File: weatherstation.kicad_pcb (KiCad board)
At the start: 2 copper layers, 126 parts, among them J1 Conn_02x05_Odd_Even, J2 Conn_02x10_Odd_Even, Q1 NX3020NAK, Q2 NX3020NAK, Q3 FDS86267P, Q4 TN2404K-T1-E3, SW1 SW_Push, U1 IS25LP064A-JBLE, U10 74AHC1G04, U11 ISL3330, U12 CPC1017N, U13 CPC1017N, U14 LM22675, U15 TPS793333-EP, U16 TPS54202, U2 MAX3221ECPWR, U3 STM32F091C(B-C)Tx_u, U4 LIS2DE12, U5 ADS1120-PW, U6 2SMPB-02E, U7 SHT3x-DIS, U8 ADA4528-1, U9 MCP2542-E/SN, X1 DSC1001CI1-004.0960T, Y1 8MHz, Y2 32.768kHz

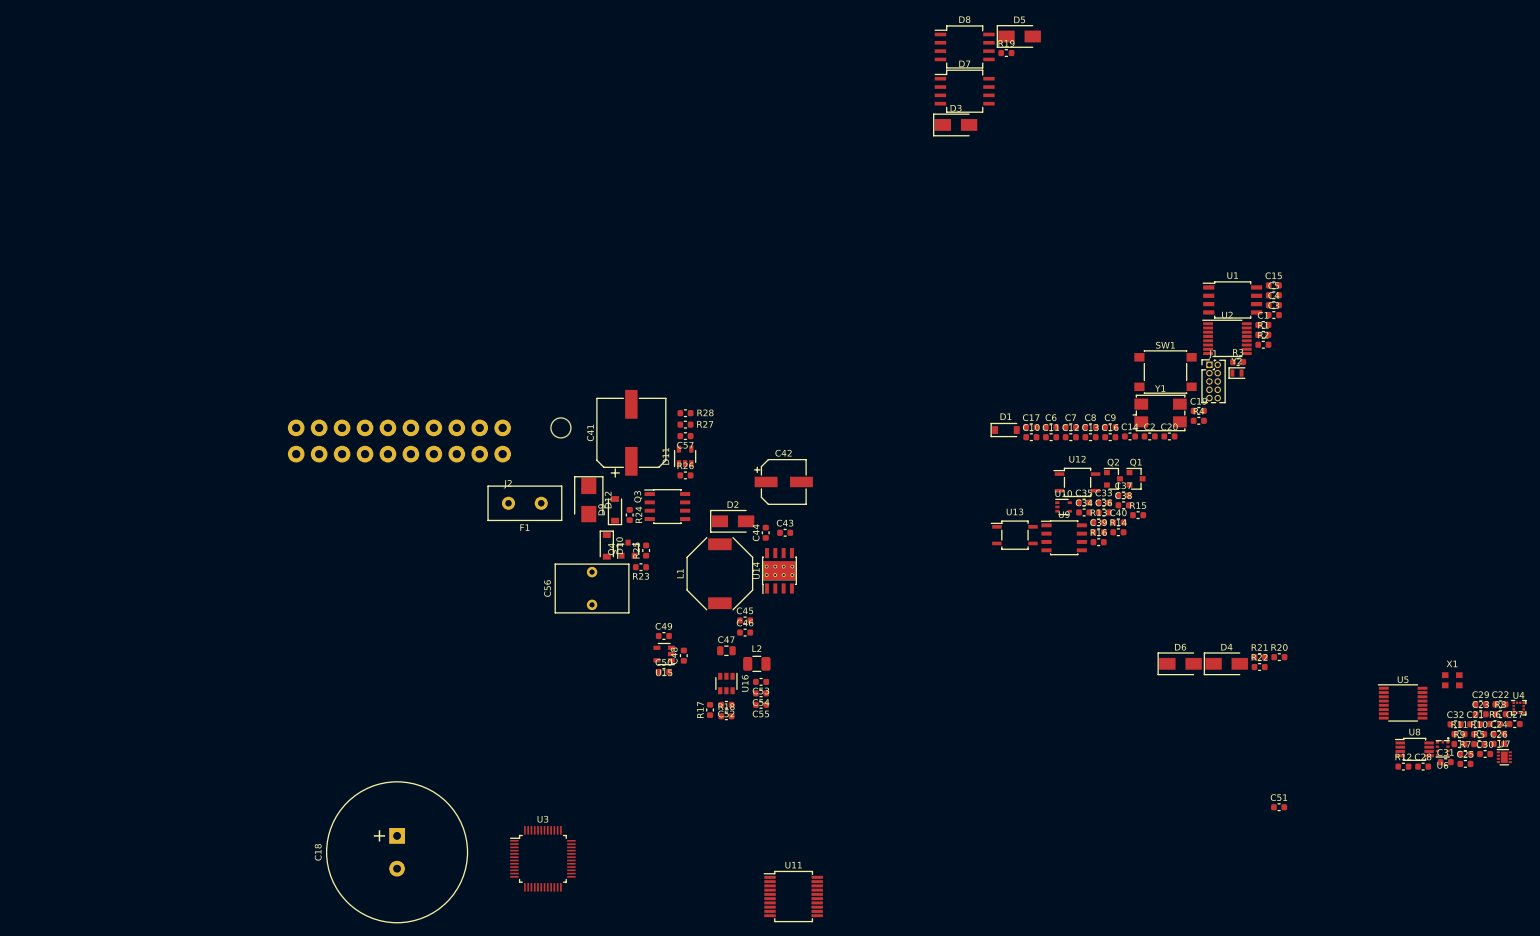
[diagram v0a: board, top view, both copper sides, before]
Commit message: Initial schematic work for rock64 version
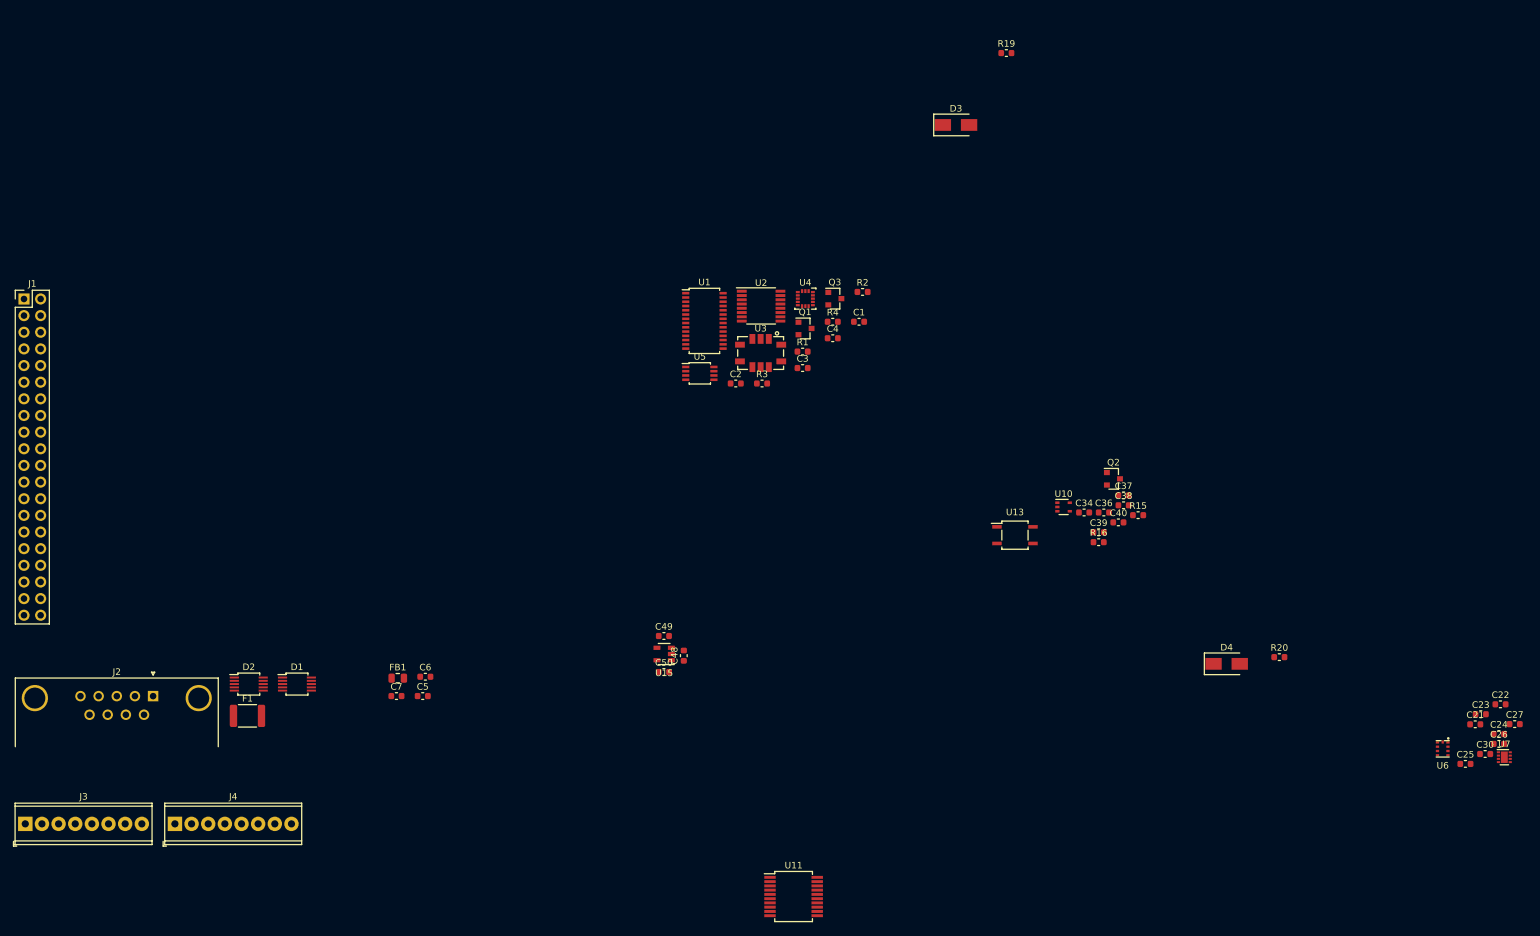
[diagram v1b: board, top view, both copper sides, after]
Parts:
- removed C10, C15, C19, C28, C32, C33, C35, C51, C57, C8, C9: 100nF, Capacitor_SMD:C_0603_1608Metric
- removed C11, C14: 26pF, Capacitor_SMD:C_0603_1608Metric
- removed C12, C29, C43: 1uF, Capacitor_SMD:C_0603_1608Metric
- removed C13, C44: 10nF, Capacitor_SMD:C_0603_1608Metric
- removed C16: 4.7uF, Capacitor_SMD:C_0603_1608Metric
- removed C17, C20: 2pF, Capacitor_SMD:C_0603_1608Metric
- removed C18: 1F, supercap:CP_Radial_D21.5mm_P5.00mm
- removed C31: 10pF, Capacitor_SMD:C_0603_1608Metric
- removed C41: 180uF, Capacitor_SMD:CP_Elec_10x12.6
- removed C42: 47uF, Capacitor_SMD:CP_Elec_6.3x7.7
- removed C45, C46, C53, C54, C55: 22uF, Capacitor_SMD:C_0603_1608Metric
- removed C47: 33uF, Capacitor_SMD:C_0805_2012Metric
- removed C52: 56pF, Capacitor_SMD:C_0603_1608Metric
- removed C56: 10uF, Capacitor_THT:C_Rect_L7.2mm_W11.0mm_P5.00mm_FKS2_FKP2_MKS2_MKP2
- removed D10, D9: PDZ5.6BGWJ, Diode_SMD:D_SOD-123
- removed D11: TL431DBV, Package_TO_SOT_SMD:SOT-23-5
- removed D12: STPS3170UF, Diode_SMD:D_SMB
- removed D5, D6: WE_824501361, Diode_SMD:D_SMA
- removed D7, D8: CM1213A-06SO, Package_SO:SO-8_5.3x6.2mm_P1.27mm
- removed L1: 33uH, inductor_sru1048:L_Bourns_SRU1048
- removed L2: 4.7uH, inductor_1008_2520:L_1008_2520Metric
- removed Q4: TN2404K-T1-E3, Package_TO_SOT_SMD:SOT-23
- removed R10, R11, R18, R8, R9: 100k, Resistor_SMD:R_0603_1608Metric
- removed R12: 1k, Resistor_SMD:R_0603_1608Metric
- removed R13: 2.1k, Resistor_SMD:R_0603_1608Metric
- removed R14: 84.5, Resistor_SMD:R_0603_1608Metric
- removed R17: 22.1k, Resistor_SMD:R_0603_1608Metric
- removed R21, R22: 10, Resistor_SMD:R_0603_1608Metric
- removed R23: 15k, Resistor_SMD:R_0603_1608Metric
- removed R24, R25, R26, R28, R7: 10k, Resistor_SMD:R_0603_1608Metric
- removed R27: 68k, Resistor_SMD:R_0603_1608Metric
- removed R5: 1, Resistor_SMD:R_0603_1608Metric
- removed R6: 23k, Resistor_SMD:R_0603_1608Metric
- removed SW1: SW_Push, Button_Switch_SMD:SW_SPST_PTS645
- removed U12: CPC1017N, Package_SO:SOP-4_3.8x4.1mm_P2.54mm
- removed U14: LM22675, Package_SO:Texas_HSOP-8-1EP_3.9x4.9mm_P1.27mm_ThermalVias
- removed U16: TPS54202, Package_TO_SOT_SMD:SOT-23-6
- removed U8: ADA4528-1, Package_SO:MSOP-8_3x3mm_P0.65mm
- removed U9: MCP2542-E/SN, Package_SO:SOIC-8_3.9x4.9mm_P1.27mm
- removed X1: DSC1001CI1-004.0960T, Oscillator:Oscillator_SMD_EuroQuartz_XO32-4Pin_3.2x2.5mm
- removed Y1: 8MHz, Crystal:Crystal_SMD_7050-4Pin_7.0x5.0mm
- removed Y2: 32.768kHz, Crystal:Crystal_SMD_2012-2Pin_2.0x1.2mm
- added FB1: 180R/100M, Inductor_SMD:L_0805_2012Metric, F.Cu at (105.6, 130.7)
- added J3: Screw_Terminal_01x08, TerminalBlock_Phoenix:TerminalBlock_Phoenix_MPT-0,5-8-2.54_1x08_P2.54mm_Horizontal, F.Cu at (48.8, 152.9)
- added J4: Screw_Terminal_01x08, TerminalBlock_Phoenix:TerminalBlock_Phoenix_MPT-0,5-8-2.54_1x08_P2.54mm_Horizontal, F.Cu at (71.6, 152.9)
- C2: value 100nF -> 4.7uF
- C21: value 10uF -> 4.7uF
- C5, C6: value 100nF -> 22uF
- C7: value 4.7uF -> 100nF
- D1: value BAT54GW -> CM1213A-08SO; footprint Diode_SMD:D_SOD-123 -> Package_SO:MSOP-10_3x3mm_P0.5mm
- D2: value MBRA160T3G -> CM1213A-08SO; footprint Diode_SMD:D_SMA -> Package_SO:MSOP-10_3x3mm_P0.5mm
- F1: value 0ZRC0160FF1A -> PFMF.030.2; footprint Capacitor_THT:C_Disc_D11.0mm_W5.0mm_P5.00mm -> Resistor_SMD:R_1812_4532Metric
- J1: value Conn_02x05_Odd_Even -> Conn_02x20_Odd_Even; footprint Connector_PinHeader_1.27mm:PinHeader_2x05_P1.27mm_Vertical -> Connector_PinHeader_2.54mm:PinHeader_2x20_P2.54mm_Vertical
- J2: value Conn_02x10_Odd_Even -> DB9_Female_MountingHoles; footprint cinch_enclosure:Cinch_ 5810120011_large -> Connector_Dsub:DSUB-9_Female_Horizontal_P2.77x2.84mm_EdgePinOffset4.94mm_Housed_MountingHolesOffset7.48mm
- Q3: value FDS86267P -> PMV160UP; footprint Package_SO:SOIC-8_3.9x4.9mm_P1.27mm -> Package_TO_SOT_SMD:SOT-23
- R1: value 100k -> 237k 0.1%
- R16: value 84.5 -> 113
- R2: value 1k -> 82
- R3: value 221 -> 51
- R4: value 10k -> 82
- U1: value IS25LP064A-JBLE -> ADS1148-PW; footprint Package_SO:SOIJ-8_5.3x5.3mm_P1.27mm -> Package_SO:TSSOP-28_4.4x9.7mm_P0.65mm
- U15: value TPS793333-EP -> TPS793285-EP
- U2: value MAX3221ECPWR -> ADS112C04-PW
- U3: value STM32F091C(B-C)Tx_u -> MICS-4514; footprint Package_QFP:LQFP-48_7x7mm_P0.5mm -> MICS-4514:MICS-4514
- U4: value LIS2DE12 -> MMA8451Q; footprint Package_LGA:LGA-12_2x2mm_P0.5mm -> Package_LGA:LGA-16_3x3mm_P0.5mm_LayoutBorder3x5y
- U5: value ADS1120-PW -> LM75C; footprint Package_SO:TSSOP-16_4.4x5mm_P0.65mm -> Package_SO:TSSOP-8_3x3mm_P0.65mm
- moved J1 181.1 mm to (48.6, 72.8)
- moved C5 143.5 mm to (109.4, 133.4)
- moved U4 125.5 mm to (167.8, 72.8)
- moved U5 118.5 mm to (151.7, 84.2)
- moved D1 114.9 mm to (90.2, 131.6)
- moved C7 110.8 mm to (105.4, 133.4)
- moved C6 102.8 mm to (109.8, 130.5)
- moved U3 84.0 mm to (161.0, 81.1)
- moved U1 80.7 mm to (152.4, 76.2)
- moved D2 77.9 mm to (82.9, 131.6)
- moved J2 74.5 mm to (68.3, 133.4)
- moved R3 72.7 mm to (161.2, 85.7)
- moved C3 72.4 mm to (167.4, 83.4)
- moved U2 71.3 mm to (161.0, 73.9)
- moved R1 70.3 mm to (167.4, 80.9)
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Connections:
- C1 pad 1: Net-(C1-Pad1) -> +3V3
- C1 pad 2: Net-(C1-Pad2) -> GND
- C2 pad 2: Net-(C2-Pad2) -> GND
- C21 pad 1: +3.3VA -> +2V8
- C22 pad 1: +3.3VA -> +3V3
- C23 pad 1: +3.3VA -> Net-(C23-Pad1)
- C25 pad 1: +3.3VA -> +2V8
- C26 pad 1: +3.3VA -> +2V8
- C27 pad 1: +3.3VA -> +3V3
- C3 pad 1: +3V3 -> +2V8
- C4 pad 1: Net-(C4-Pad1) -> +3.3VA
- C48 pad 1: +5V -> +2V8
- C5 pad 1: Net-(C5-Pad1) -> +3.3VA
- C6 pad 1: +3V3 -> +3.3VA
- C7 pad 1: +3V3 -> +3.3VA
- D1 pad 1: Net-(D1-Pad1) -> (no net)
- D1 pad 2: +3V3 -> (no net)
- D2 pad 1: Net-(C44-Pad1) -> IEXC1
- D2 pad 2: GND -> IEXC2
- F1 pad 2: +VDC -> +5V
- J1 pad 10: /nRST -> (no net)
- J1 pad 2: /SWDIO -> +5V
- J1 pad 3: GND -> I2C0_SDA
- J1 pad 4: /SWCLK -> +5V
- J1 pad 5: GND -> I2C0_SCL
- J1 pad 6: Net-(J1-Pad6) -> GND
- J1 pad 7: Net-(J1-Pad7) -> (no net)
- J1 pad 8: Net-(J1-Pad8) -> (no net)
- J2 pad 1: +VDC -> (no net)
- J2 pad 2: GND -> /connectors/RS485_D-_ESD
- J2 pad 3: /connectors/CAN_H_ESD -> /connectors/RS485_D+_ESD
- J2 pad 4: /connectors/CAN_L_ESD -> (no net)
- J2 pad 5: /connectors/RS485_D-_ESD -> GND
- J2 pad 6: /connectors/RS485_D+_ESD -> (no net)
- J2 pad 7: DBG_TX -> (no net)
- J2 pad 8: DBG_RX -> (no net)
- J2 pad 9: ADC_IN6 -> (no net)
- Q1 pad 1: CAN_TERM -> SNSR_HEAT
- Q3 pad 1: Net-(C41-Pad1) -> ~SNSR_HEAT2
- Q3 pad 2: Net-(C41-Pad1) -> Net-(Q3-Pad2)
- Q3 pad 3: Net-(C41-Pad1) -> Net-(Q3-Pad3)
- R1 pad 1: CAN_STBY -> /sensors/afe/RsRED_Isrc
- R2 pad 1: Net-(D1-Pad1) -> +5V
- R2 pad 2: Net-(C18-Pad1) -> Net-(R2-Pad2)
- R3 pad 1: /RCC_OSC_OUT -> Net-(Q3-Pad2)
- R3 pad 2: Net-(C14-Pad1) -> Net-(Q3-Pad3)
- R4 pad 1: +3V3 -> +5V
- R4 pad 2: /nRST -> Net-(Q3-Pad2)
- U1 pad 1: SPI1_NSS -> +3V3
- U1 pad 2: SPI1_MISO -> GND
- U1 pad 3: +3V3 -> (no net)
- U1 pad 4: GND -> +3V3
- U1 pad 5: SPI1_MOSI -> REFP0
- U1 pad 6: SPI1_SCK -> REFN1
- U1 pad 7: +3V3 -> REFP1
- U1 pad 8: +3V3 -> REFN0
- U11 pad 15: USART2_TX -> (no net)
- U15 pad 1: +5V -> +2V8
- U15 pad 3: +5V -> +2V8
- U2 pad 10: Net-(U2-Pad10) -> /sensors/afe/RsOX_Isrc
- U2 pad 11: USART1_TX -> /sensors/afe/RsOX_Isrc
- U2 pad 12: GND -> +2V8
- U2 pad 13: DBG_TX -> +3V3
- U2 pad 14: GND -> ~DRDY_SNSR
- U2 pad 15: +3V3 -> I2C0_SCL
- U2 pad 16: +3V3 -> I2C0_SDA
- U2 pad 2: Net-(C1-Pad1) -> GND
- U2 pad 3: Net-(C4-Pad1) -> +3V3
- U2 pad 4: Net-(C1-Pad2) -> GND
- U2 pad 5: Net-(C2-Pad1) -> GND
- U2 pad 6: Net-(C2-Pad2) -> /sensors/afe/RsRED_Isrc
- U2 pad 7: Net-(C5-Pad1) -> /sensors/afe/RsRED_Isrc
- U2 pad 8: DBG_RX -> (no net)
- U2 pad 9: USART1_RX -> (no net)
- U4 pad 1: I2C1_SCL -> +3V3
- U4 pad 10: +3.3VA -> GND
- U4 pad 11: Net-(U4-Pad11) -> INT1_ACCEL
- U4 pad 12: INT1_ACCEL -> GND
- U4 pad 2: +3.3VA -> Net-(C23-Pad1)
- U4 pad 3: GND -> (no net)
- U4 pad 4: I2C1_SDA -> I2C0_SCL
- U4 pad 6: GND -> I2C0_SDA
- U4 pad 8: GND -> (no net)
- U4 pad 9: +3.3VA -> (no net)
- U5 pad 1: SPI2_SCK -> I2C0_SDA
- U5 pad 2: SPI2_NSS -> I2C0_SCL
- U5 pad 3: Net-(U5-Pad3) -> (no net)
- U5 pad 6: AFE_AIN3 -> GND
- U5 pad 7: AFE_AIN2 -> GND
- U5 pad 8: Net-(U5-Pad8) -> +3.3VA
- U6 pad 3: I2C1_SDA -> I2C0_SDA
- U6 pad 4: I2C1_SCL -> I2C0_SCL
- U6 pad 6: +3.3VA -> +3V3
- U6 pad 9: Net-(U6-Pad9) -> (no net)
- U7 pad 1: I2C1_SDA -> I2C0_SDA
- U7 pad 4: I2C1_SCL -> I2C0_SCL

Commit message: Revision A
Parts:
- removed C34: 100nF, Capacitor_SMD:C_0603_1608Metric
- removed U10: 74AHC1G04, Package_TO_SOT_SMD:SOT-353_SC-70-5
- added H1: MountingHole_Pad, MountingHole:MountingHole_2.7mm_M2.5_ISO14580_Pad, F.Cu at (33.5, 23.5)
- added H2: MountingHole_Pad, MountingHole:MountingHole_2.7mm_M2.5_ISO14580_Pad, F.Cu at (91.5, 23.5)
- added H3: MountingHole_Pad, MountingHole:MountingHole_2.7mm_M2.5_ISO14580_Pad, F.Cu at (91.5, 72.5)
- added H4: MountingHole_Pad, MountingHole:MountingHole_2.7mm_M2.5_ISO14580_Pad, F.Cu at (33.5, 72.5)
- added J5: Conn_02x11_Odd_Even, Connector_PinHeader_2.54mm:PinHeader_2x11_P2.54mm_Vertical, F.Cu at (43.6, 30.4)
- moved C24 228.9 mm to (60.5, 55.8), turned to 270 degrees
- moved R20 215.4 mm to (42.2, 42.2)
- moved C25 215.2 mm to (70.4, 59.7)
- moved C22 211.9 mm to (75.8, 59.2), turned to 270 degrees
- moved C21 210.9 mm to (75.8, 55.4), turned to 90 degrees
- moved C23 207.6 mm to (77.6, 60.2), turned to 270 degrees
- moved U7 205.7 mm to (85.7, 61.0)
- moved C26 205.0 mm to (87.0, 55.8), turned to 180 degrees
- moved C27 205.0 mm to (89.2, 53.2), turned to 270 degrees
- moved D4 204.6 mm to (47.5, 40.2), turned to 270 degrees
- moved C30 199.8 mm to (89.0, 61.0), turned to 90 degrees
- moved U6 198.8 mm to (87.0, 53.0), turned to 180 degrees
- moved R16 183.9 mm to (42.2, 40.5), turned to 180 degrees
- moved R15 182.8 mm to (50.9, 33.1)
- moved Q2 179.9 mm to (47.5, 34.2), turned to 180 degrees
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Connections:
- D1 pad 1: (no net) -> AFE_AIN0
- D1 pad 10: REFN1 -> REFP0
- D1 pad 2: (no net) -> AFE_AIN1
- D1 pad 3: AFE_AIN6 -> AFE_AIN4
- D1 pad 4: AFE_AIN7 -> AFE_AIN5
- D1 pad 6: REFP0 -> REFN0
- D1 pad 7: REFN0 -> REFP1
- D1 pad 9: REFP1 -> REFN1
- D2 pad 1: IEXC1 -> AFE_AIN6
- D2 pad 10: AFE_AIN5 -> IEXC2
- D2 pad 2: IEXC2 -> AFE_AIN7
- D2 pad 3: AFE_AIN0 -> AFE_AIN2
- D2 pad 4: AFE_AIN1 -> AFE_AIN3
- D2 pad 6: AFE_AIN2 -> (no net)
- D2 pad 7: AFE_AIN3 -> (no net)
- D2 pad 9: AFE_AIN4 -> IEXC1
- D3 pad 1: /connectors/RS485_D-_ESD -> COMM_RS232_TX_RS485_D-
- D4 pad 2: /connectors/RS485_D+_ESD -> COMM_RS232_RX_RS485_D+
- J1 pad 13: SNSR_HEAT -> RS485_TERM
- J1 pad 15: (no net) -> GPIO3_A4
- J1 pad 16: (no net) -> GPIO3_A5
- J1 pad 17: +3V3 -> (no net)
- J1 pad 18: (no net) -> GPIO3_A6
- J1 pad 22: INT1_ACCEL -> ~DRDY~_AFE
- J1 pad 26: ~DRDY~_AFE -> INT1_ACCEL
- J1 pad 33: RS485_TERM -> ALERT_HUMID
- J1 pad 36: ALERT_HUMID -> SNSR_HEAT
- J3 pad 3: REFN0 -> REFN1
- J3 pad 5: REFN1 -> REFN0
- J3 pad 6: AFE_AIN7 -> AFE_AIN0
- J3 pad 7: AFE_AIN6 -> AFE_AIN1
- J3 pad 8: AFE_AIN5 -> AFE_AIN4
- J4 pad 1: AFE_AIN4 -> AFE_AIN5
- J4 pad 2: AFE_AIN3 -> AFE_AIN6
- J4 pad 3: AFE_AIN2 -> AFE_AIN7
- J4 pad 4: AFE_AIN1 -> AFE_AIN2
- J4 pad 5: AFE_AIN0 -> AFE_AIN3
- R16 pad 1: COMM_RS232_TX_RS485_D- -> COMM_RS232_RX_RS485_D+
- U1 pad 4: +3V3 -> ~RESET
- U11 pad 12: Net-(U10-Pad4) -> GPIO3_A5
- U11 pad 15: (no net) -> GPIO3_A4
- U11 pad 16: USART2_RX -> GPIO3_A6
- U11 pad 17: USART2_RX -> GPIO3_A6
- U11 pad 9: USART2_DE -> GPIO3_A5
- U13 pad 3: COMM_RS232_RX_RS485_D+ -> Net-(R16-Pad2)
- U13 pad 4: Net-(R16-Pad2) -> COMM_RS232_TX_RS485_D-
- U15 pad 1: +2V8 -> +3.3VA
- U15 pad 3: +2V8 -> +3.3VA
- U15 pad 5: +3.3VA -> +2V8
- U2 pad 10: /sensors/afe/RsOX_Isrc -> /sensors/afe/RsRED_Isrc
- U2 pad 11: /sensors/afe/RsOX_Isrc -> /sensors/afe/RsRED_Isrc
- U2 pad 3: +3V3 -> ~RESET
- U2 pad 6: /sensors/afe/RsRED_Isrc -> /sensors/afe/RsOX_Isrc
- U2 pad 7: /sensors/afe/RsRED_Isrc -> /sensors/afe/RsOX_Isrc
- U6 pad 1: GND -> ~RESET
- U6 pad 2: +3.3VA -> +3V3
- U6 pad 7: (no net) -> GND
- U6 pad 8: GND -> +2V8
- U7 pad 6: +3.3VA -> ~RESET
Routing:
- net +3V3: track 0.00 -> 174.6 mm, vias 0 -> 10
- net +5V: track 0.00 -> 118.2 mm, vias 0 -> 1
- net +2V8: track 0.00 -> 117.0 mm, vias 0 -> 6
- net +3.3VA: track 0.00 -> 96.4 mm, vias 0 -> 8
- net I2C0_SDA: track 0.00 -> 94.5 mm, vias 0 -> 5
- net I2C0_SCL: track 0.00 -> 94.1 mm, vias 0 -> 5
- net ~RESET: track 0.00 -> 80.1 mm, vias 0 -> 6
- net ALERT_HUMID: track 0.00 -> 52.1 mm, vias 0 -> 1
- net COMM_MODE: track 0.00 -> 48.7 mm, vias 0 -> 5
- net ~DRDY~_AFE: track 0.00 -> 42.5 mm, vias 0 -> 1
- net SPI_CSN0_M2: track 0.00 -> 40.8 mm, vias 0 -> 1
- net SPI_TXD_M2: track 0.00 -> 39.7 mm, vias 0 -> 1
- net SPI_RXD_M2: track 0.00 -> 38.6 mm, vias 0 -> 1
- net INT1_ACCEL: track 0.00 -> 38.4 mm, vias 0 -> 1
- net SPI_CLK_M2: track 0.00 -> 35.4 mm, vias 0 -> 1
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- added copper zone on B.Cu, net GND
- added copper zone on F.Cu, net GND
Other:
- board outline added: 65.3 x 56 mm
- net class Default: clearance 0.2 -> 0.1524; trace_width 0.25 -> 0.1524; via_dia 0.8 -> 0.7; via_drill 0.4 -> 0.3
- rule trace_clearance: 0.2 -> 0.1524
- rule trace_min: 0.2 -> 0.1524
- rule via_min_size: 0.4 -> 0.3
